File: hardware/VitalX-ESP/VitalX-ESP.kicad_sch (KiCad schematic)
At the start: 25 parts, among them J1 ECG Probe, U1 AD8232ACPZ-R7, U2 ESP32-WROOM-32U, U3 ADP160AUJZ-1.8-R7

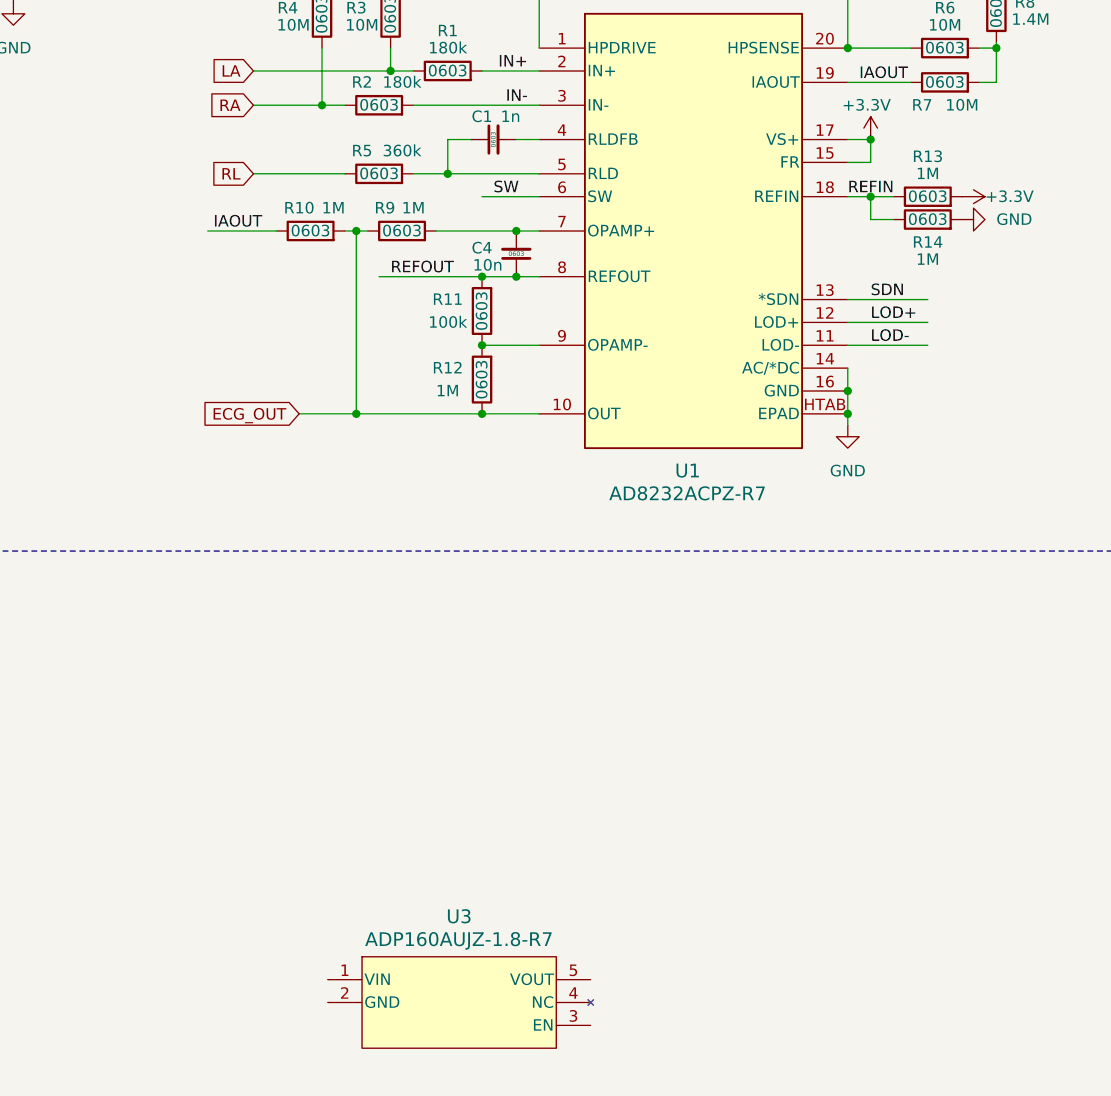
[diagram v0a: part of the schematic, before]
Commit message: [VTX-5] Finalize ECG Block. Minor changes: - Remove cache, bak files. - Change AD8232's EPAD electrical type for ERC. - Update footprint path.
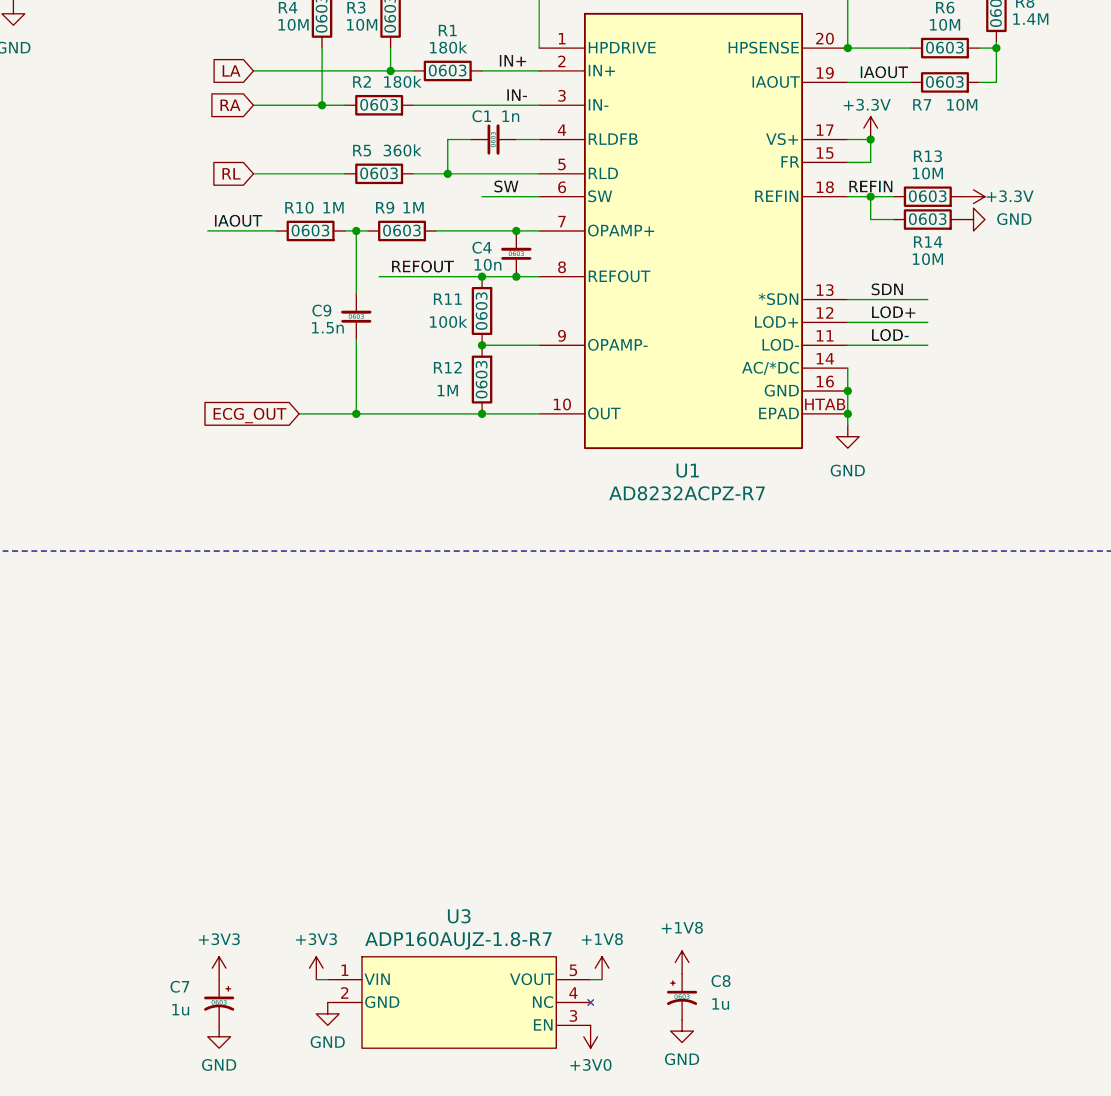
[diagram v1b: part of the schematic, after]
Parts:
- added C7, C8: 1u, Capacitor_SMD:C_0603_1608Metric, symbol Device:C_Polarized_Small_US
- added C9: 1.5n, Capacitor_SMD:C_0603_1608Metric, symbol Device:C_Small
- R13, R14: value 1M -> 10M
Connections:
- net ECG_OUT: now also C9.1; no longer R10.2, R9.1
- net GND: now also U3.2 (GND), C7.2, C8.2
- net +3V3: now reaches U3.1 (VIN)
- net +3V3: now also C7.1
- net +3V0: now reaches U3.3 (EN)
- net +1V8: now reaches U3.5 (VOUT)
- net +1V8: now also C8.1
- new net: C9.2, R10.2, R9.1

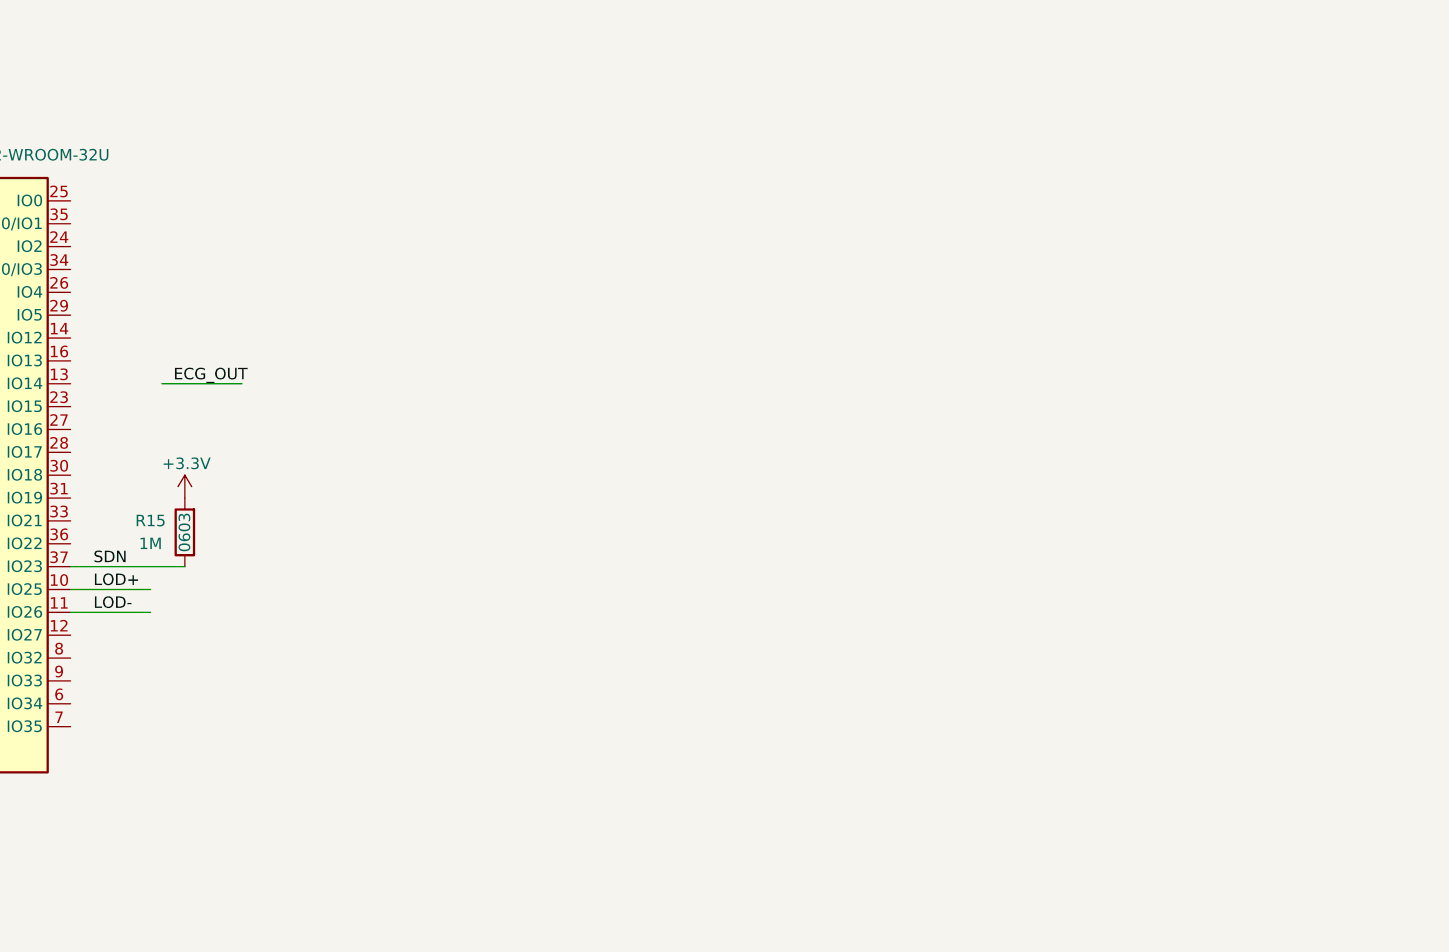
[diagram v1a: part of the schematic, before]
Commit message: [VTX-6] Initialize PPG Block.
Initial implementation of ADPD144RI.
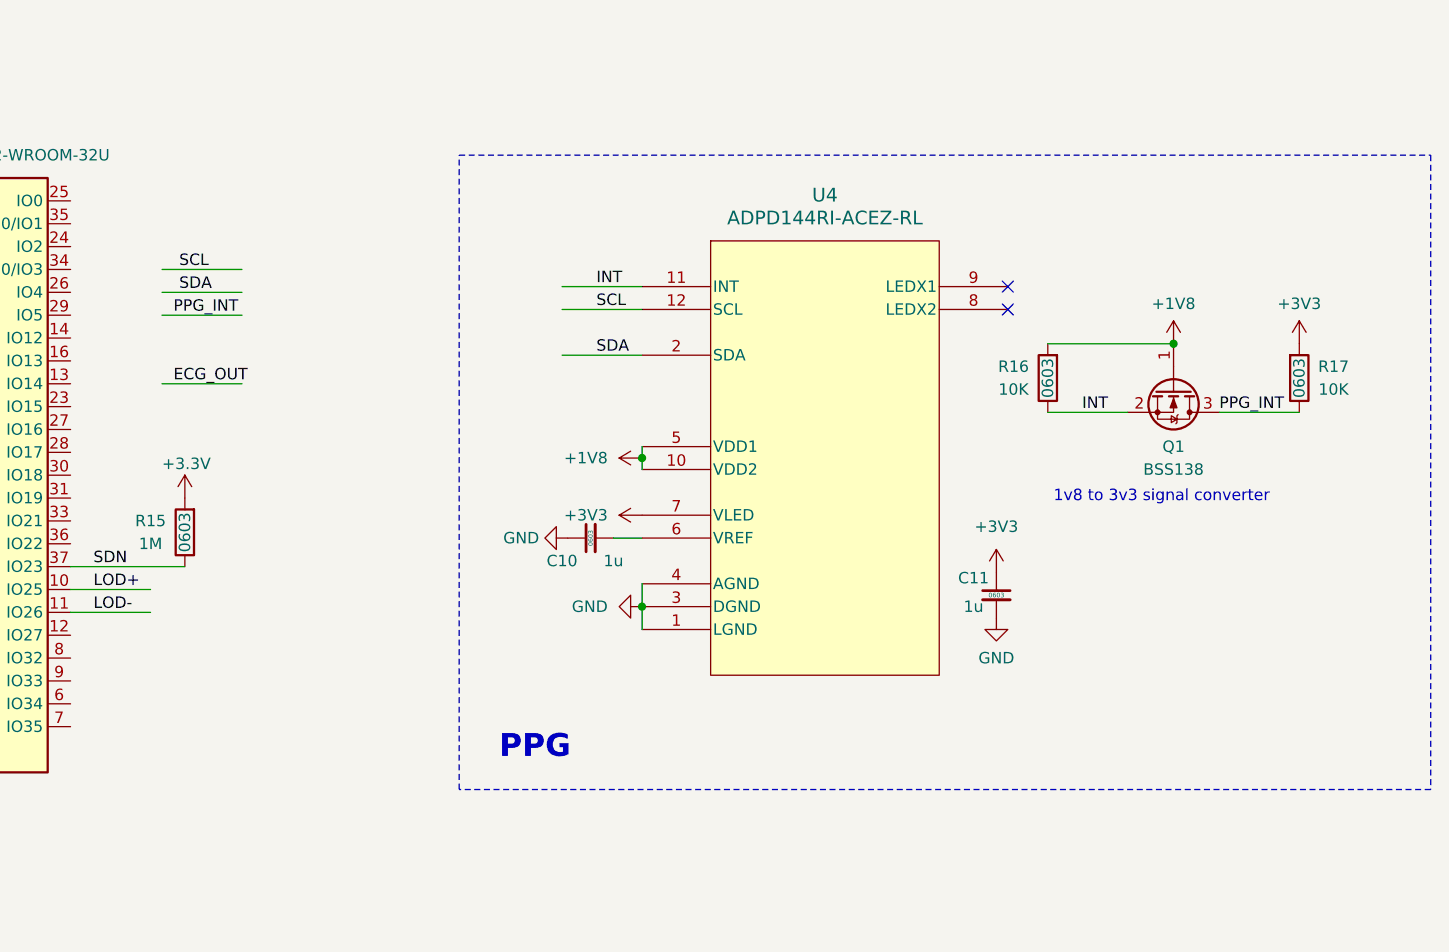
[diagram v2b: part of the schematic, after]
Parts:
- added C10, C11: 1u, Capacitor_SMD:C_0603_1608Metric, symbol Device:C_Small
- added Q1: BSS138, Package_TO_SOT_SMD:SOT-23, symbol Transistor_FET:BSS138
- added R16, R17: 10K, Resistor_SMD:R_0603_1608Metric, symbol Device:R
- added U4: ADPD144RI-ACEZ-RL, CE-12-2_ADI, symbol ADPD144RI:ADPD144RI-ACEZ-RL
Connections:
- net +1V8: now also Q1.1 (G), R16.2, U4.10 (VDD2), U4.5 (VDD1)
- net +3V3: now also C11.1, R17.2, U4.7 (VLED)
- net GND: now also C10.1, C11.2, U4.1 (LGND), U4.3 (DGND), U4.4 (AGND)
- new net: C10.2, U4.6 (VREF)
- new net INT: Q1.2 (S), R16.1, U4.11 (INT)
- new net PPG_INT: Q1.3 (D), R17.1
- new net SCL: U4.12 (SCL)
- new net SDA: U4.2 (SDA)
- no-connect marks 0 -> 2
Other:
- note added: "1v8 to 3v3 signal converter"
- note added: "PPG"

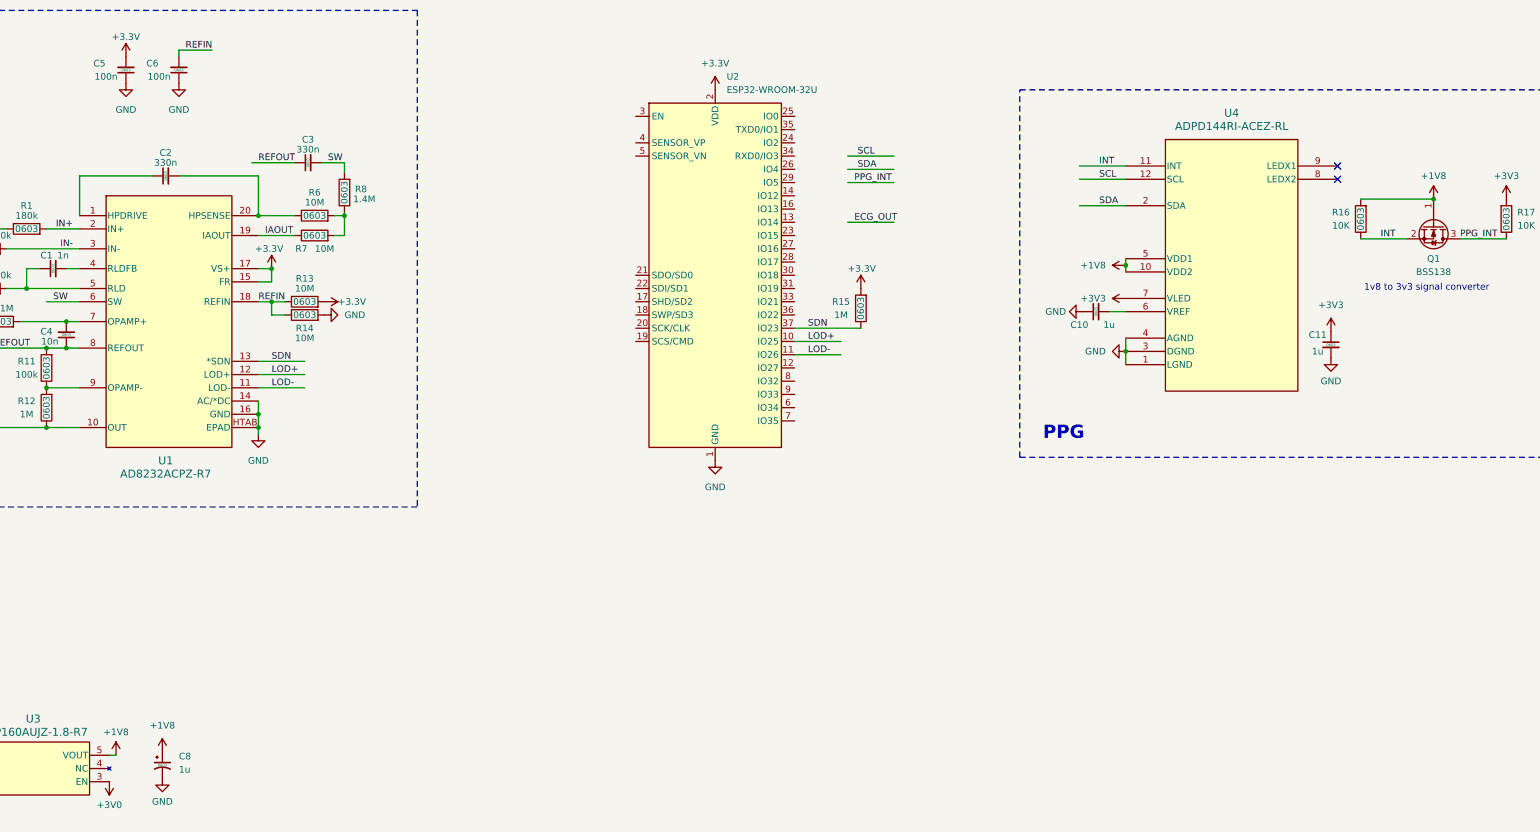
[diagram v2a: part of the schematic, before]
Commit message: [VTX-6] Finalize PPG Block.
Included AMS1117-3.3V voltage regulator.
Increased Vled capacitor from 1uF to 10uF.
Pull up resistor on ADPD144RI I2C line.
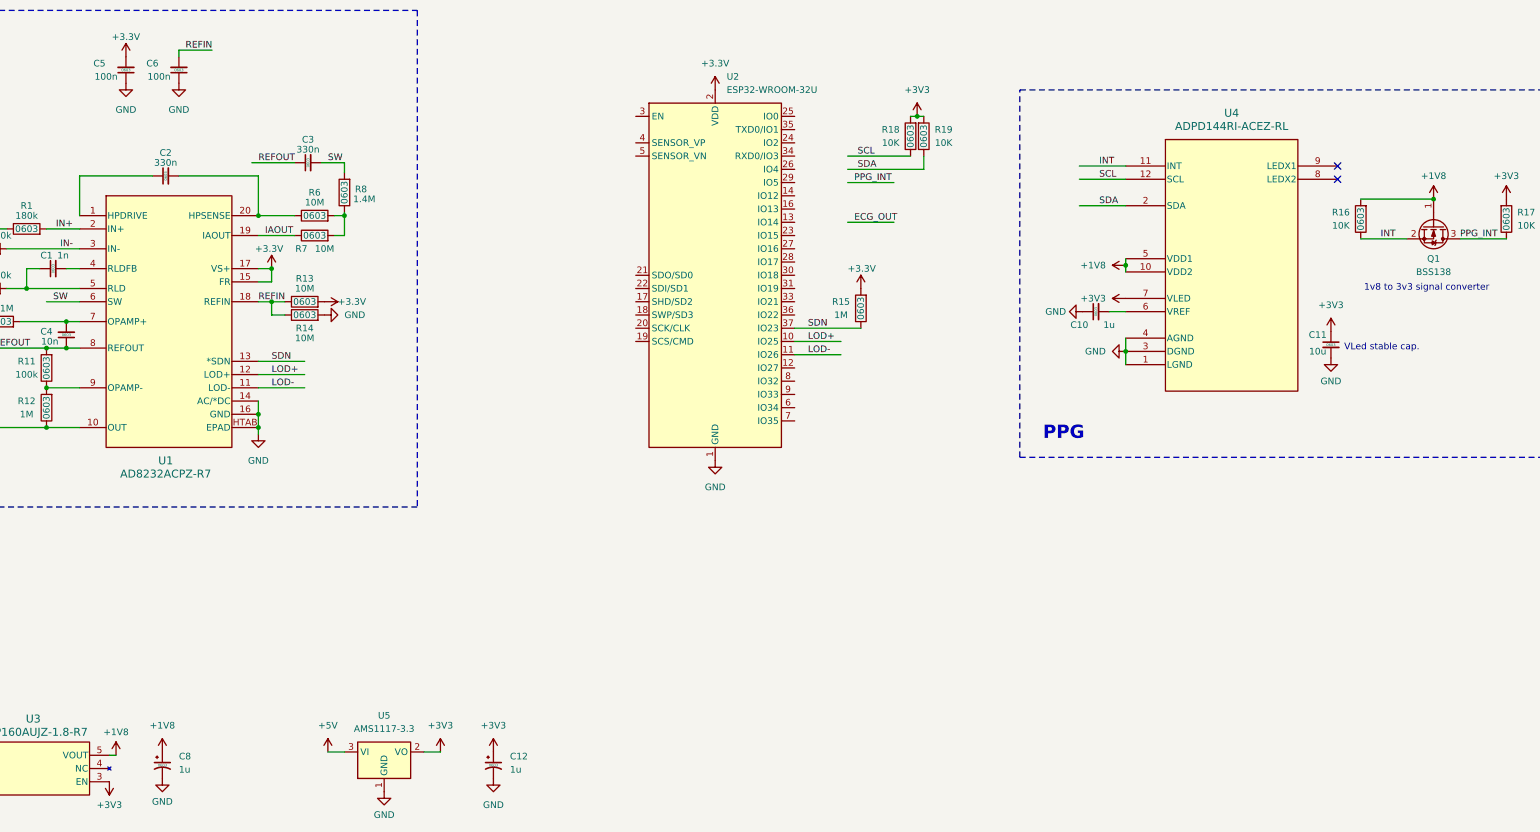
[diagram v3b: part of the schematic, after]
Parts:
- added C12: 1u, Capacitor_SMD:C_0603_1608Metric, symbol Device:C_Polarized_Small_US
- added R18, R19: 10K, Resistor_SMD:R_0603_1608Metric, symbol Device:R
- added U5: AMS1117-3.3, Package_TO_SOT_SMD:SOT-223-3_TabPin2, symbol Regulator_Linear:AMS1117-3.3
- C11: value 1u -> 10u
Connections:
- net +3V0 is gone; now on net +3V3: U3.3 (EN)
- net +3V3: now also C12.1, R18.2, R19.2, U5.2 (VO)
- net GND: now also C12.2, U5.1 (GND)
- net SCL: now also R18.1
- net SDA: now also R19.1
- new net +5V: U5.3 (VI)
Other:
- note added: "VLed stable cap."

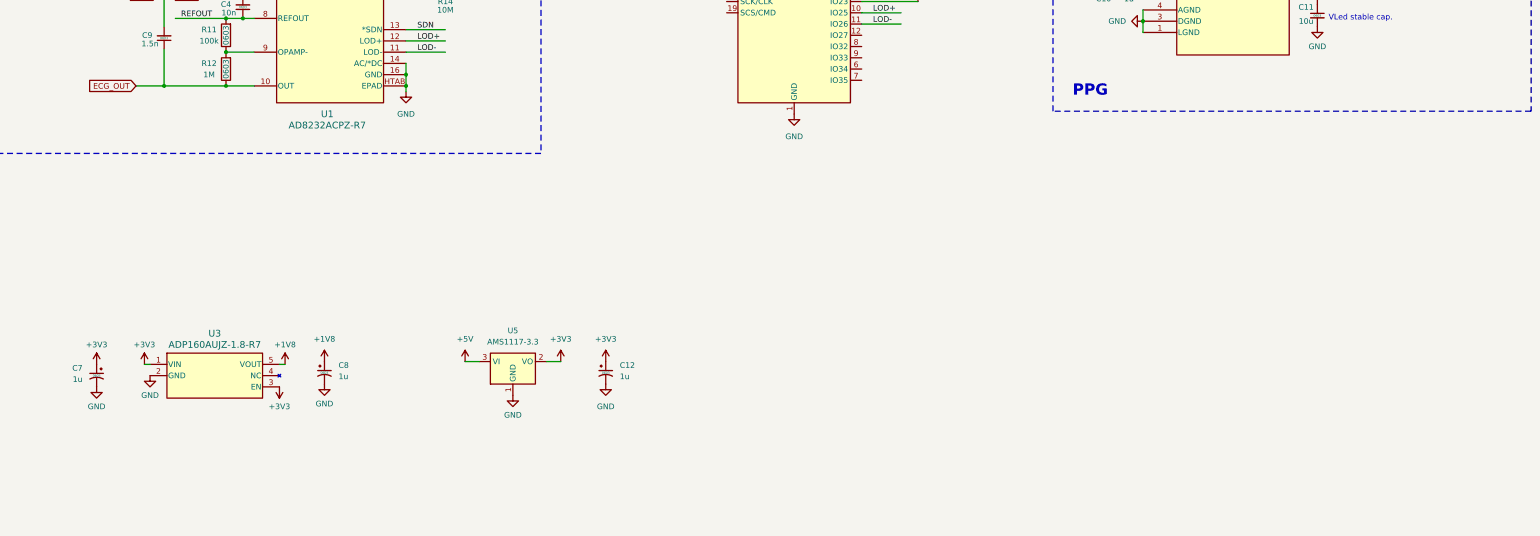
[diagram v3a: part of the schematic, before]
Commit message: [VTX-7] Initialize GSR Block.
Initial implementation of GSR/EDA readout circuit.
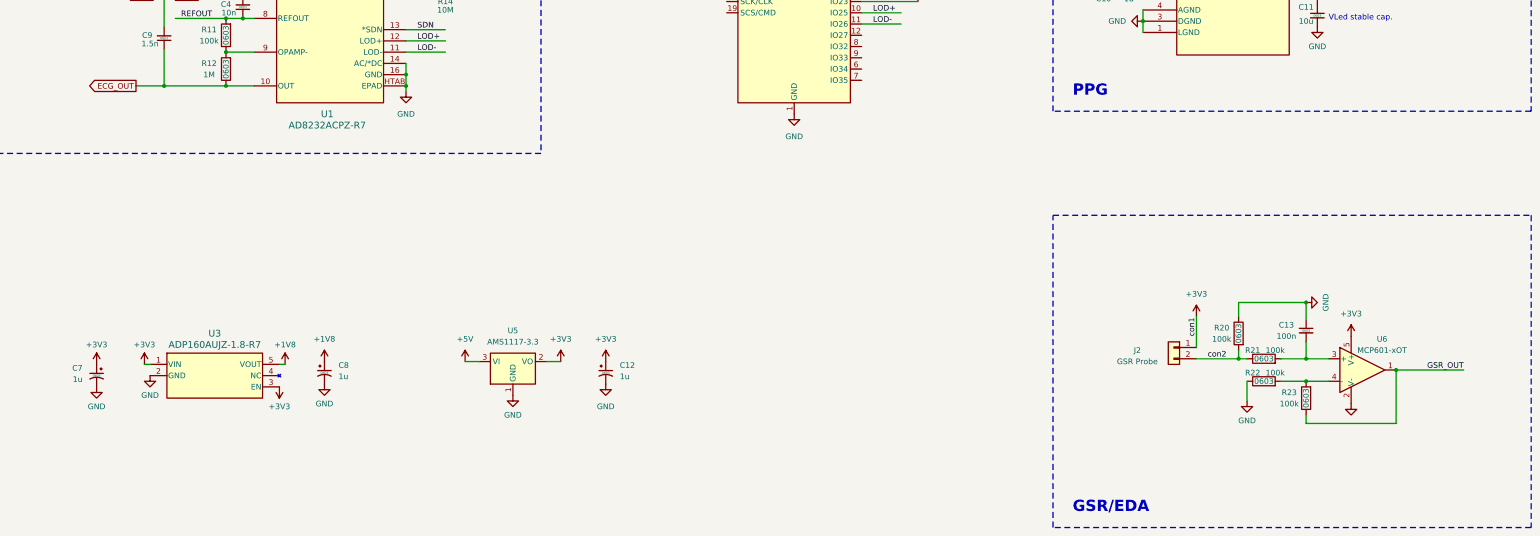
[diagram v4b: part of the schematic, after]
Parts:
- added C13: 100n, Capacitor_SMD:C_0603_1608Metric, symbol Device:C_Small
- added J2: GSR Probe, Connector_PinHeader_2.54mm:PinHeader_1x02_P2.54mm_Vertical_SMD_Pin1Left, symbol Connector_Generic:Conn_01x02
- added R20, R21, R22, R23: 100k, Resistor_SMD:R_0603_1608Metric, symbol Device:R
- added U6: MCP601-xOT, Package_TO_SOT_SMD:SOT-23-5, symbol Amplifier_Operational:MCP601-xOT
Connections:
- net +3V3: now also J2.1 (Pin_1), U6.5 (V+)
- net GND: now also C13.1, R20.1, R22.1, U6.2 (V-)
- new net: C13.2, R21.2, U6.3 (+)
- new net: R22.2, R23.2, U6.4 (-)
- new net GSR_OUT: R23.1, U6.1
- new net con2: J2.2 (Pin_2), R20.2, R21.1
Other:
- note added: "GSR/EDA"
